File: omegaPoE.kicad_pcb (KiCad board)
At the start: 4 copper layers, 34 x 48 mm, 75 parts, among them J1 RJ45-TRANS_POE, J2 CONN_EXPANSION, J3 Conn_02x01, J4 Conn_02x01, Q1 FDM3622, SW1 SW_Push, T1 PA1276, U1 LM5070, U2 PS2501-1, U3 ONION-OMEGA2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

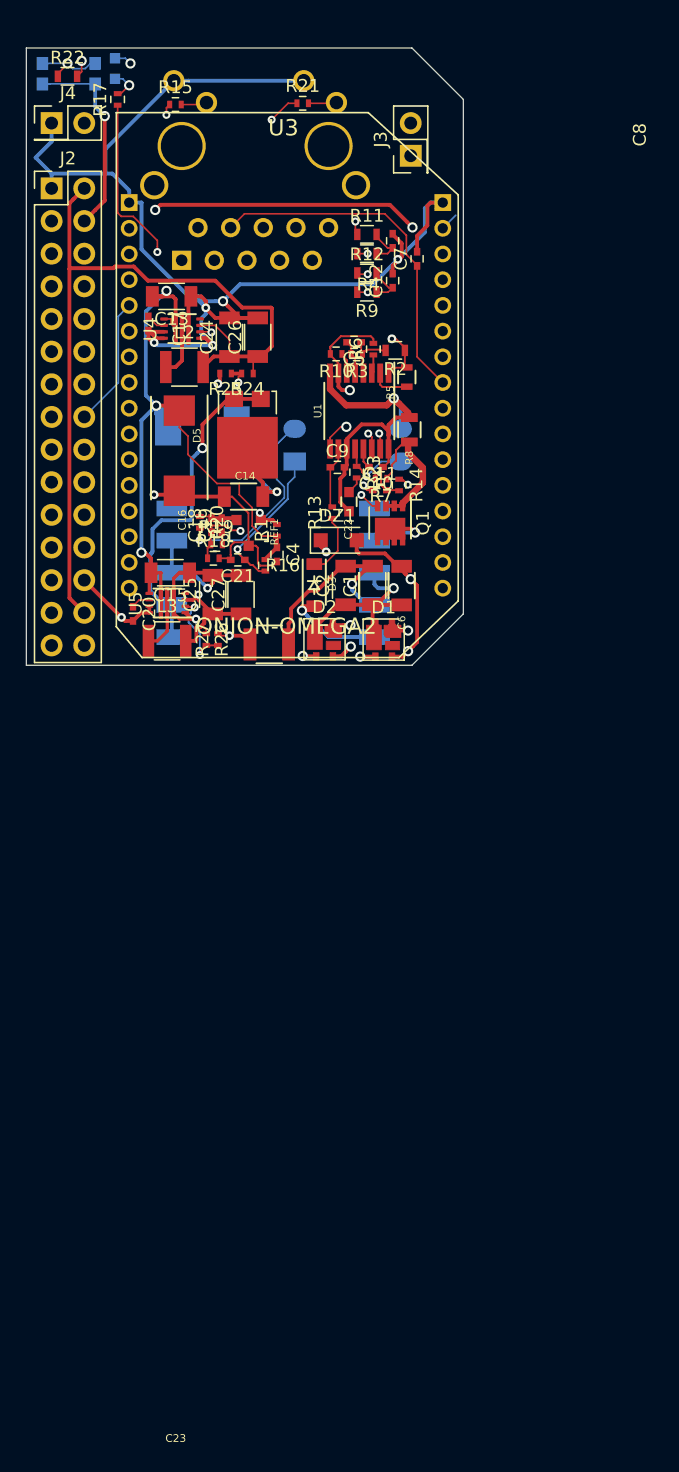
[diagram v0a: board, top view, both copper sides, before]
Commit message: More cleanup, some power planes in and text fixed
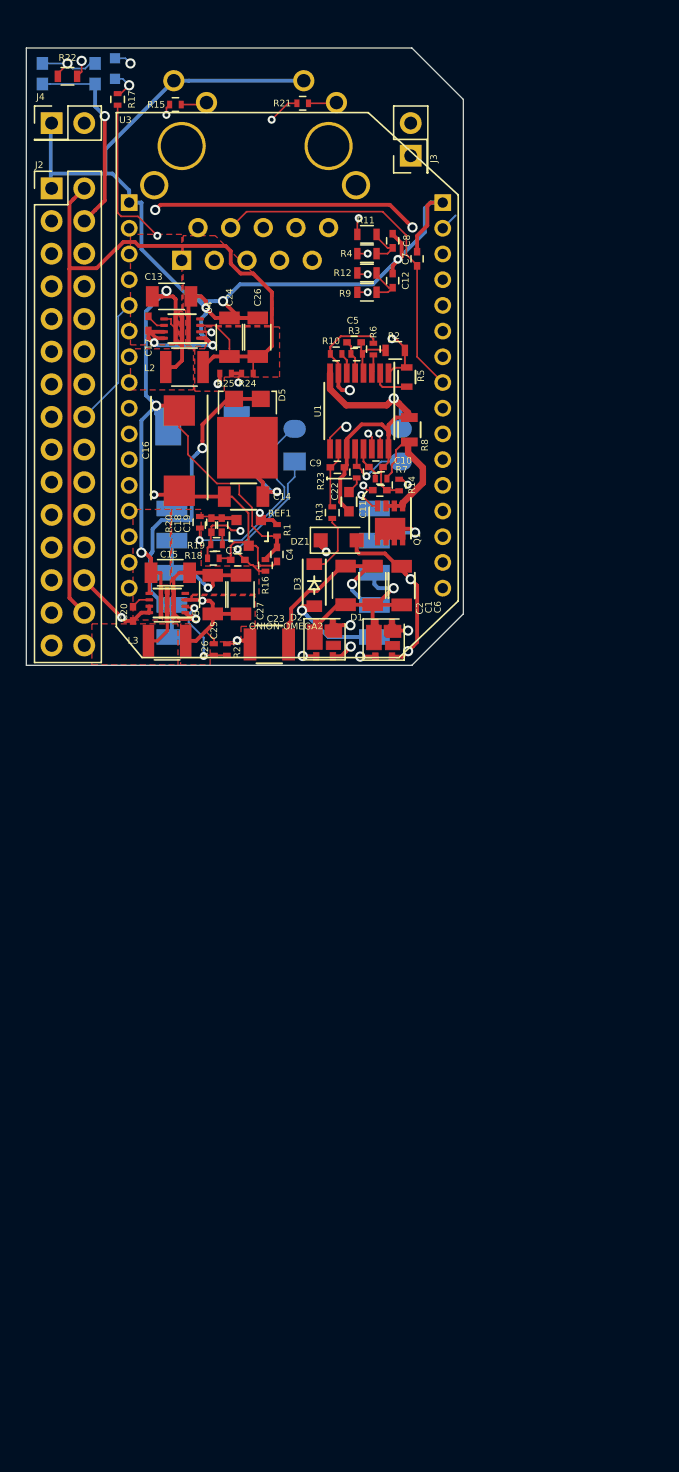
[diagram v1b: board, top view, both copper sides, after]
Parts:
- moved R27 1.04 mm to (98.6, 98.3)
- moved R26 0.98 mm to (97.6, 98.3)
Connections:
- J2 pad 5: Net-(J2-Pad5) -> (no net)
- U4 pad 7: (no net) -> Net-(U4-Pad7)
- U5 pad 7: (no net) -> Net-(U5-Pad7)
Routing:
- net /D+: track 31.5 -> 35.5 mm
- net +5V: track 65.6 -> 68.5 mm
- net /ETH_TD-: track 31.7 -> 33.6 mm
- net /ETH_TD+: track 35.8 -> 37.7 mm
- net /IO12: track 38.7 -> 40.4 mm
- net /D-: track 34.0 -> 35.3 mm
- net /ETH_RD+: track 33.2 -> 32.1 mm
- net /IO13: track 48.7 -> 49.7 mm
- net GND: track 196.2 -> 195.7 mm
- added copper zone on F.Cu, net +12V
- added copper zone on F.Cu, net +3V3
- added copper zone on F.Cu, net +5V
- added copper zone on F.Cu, net GND
- added copper zone on In1.Cu, net GND
- added copper zone on F.Cu, net Net-(L2-Pad1)
- added copper zone on F.Cu, net Net-(L3-Pad1)
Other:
- rule pad_to_mask_clearance: 0 -> 0.05
- rule via_min_size: 0.625 -> 0.56

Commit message: Mostly finished with design. Fixed lots of 3D models and some part rotations.
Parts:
- C16: footprint Capacitors_Tantalum_SMD:TantalC_SizeD_EIA-7343_Reflow -> Capacitors_Tantalum_SMD:CP_Tantalum_Case-D_EIA-7343-31_Reflow
- D1, D2: value D_Bridge_+-AA -> D_Bridge_A+A-
- D3: footprint Diodes_SMD:SOD-123 -> Diodes_SMD:D_SOD-123
- J3: moved to B.Cu
- L1: footprint inductors:Murata-3000A-series -> lib_fp:Murata-3000A-series
- REF1: footprint Housings_SOT-23_SOT-143_TSOT-6:SOT-23 -> TO_SOT_Packages_SMD:SOT-23
- T1: footprint ethernet_transformers:Pulse_PA1269 -> lib_fp:Pulse_PA1269
- U2: footprint DIP_Gull:DIP-Gull-4 -> Housings_DIP:SMDIP-4_W7.62mm
- moved U2 0.28 mm to (108.0, 82.1), turned to 0 degrees
- moved C18 0.14 mm to (97.3, 88.7)
- moved C19 0.14 mm to (98.1, 88.7)
- moved R19 0.14 mm to (97.7, 90.2)
- moved R20 0.14 mm to (96.4, 88.5)
- turned REF1 to 270 degrees
- turned D1 to 270 degrees
- turned D2 to 270 degrees
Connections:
- D1 pad 1: /Input_GND -> /Bridge1_2
- D1 pad 2: /Input-48V -> /Input_GND
- D1 pad 4: /Bridge1_2 -> /Input-48V
- D2 pad 1: /Input_GND -> /Bridge2_2
- D2 pad 2: /Input-48V -> /Input_GND
- D2 pad 4: /Bridge2_2 -> /Input-48V
- J2 pad 5: (no net) -> Net-(J2-Pad5)
- U4 pad 7: Net-(U4-Pad7) -> (no net)
- U5 pad 7: Net-(U5-Pad7) -> (no net)
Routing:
- net Net-(R20-Pad2): track 15.2 -> 16.9 mm
- net Net-(C21-Pad1): track 11.7 -> 12.9 mm
- net /fetdrive: track 10.1 -> 10.5 mm, vias 2 -> 0

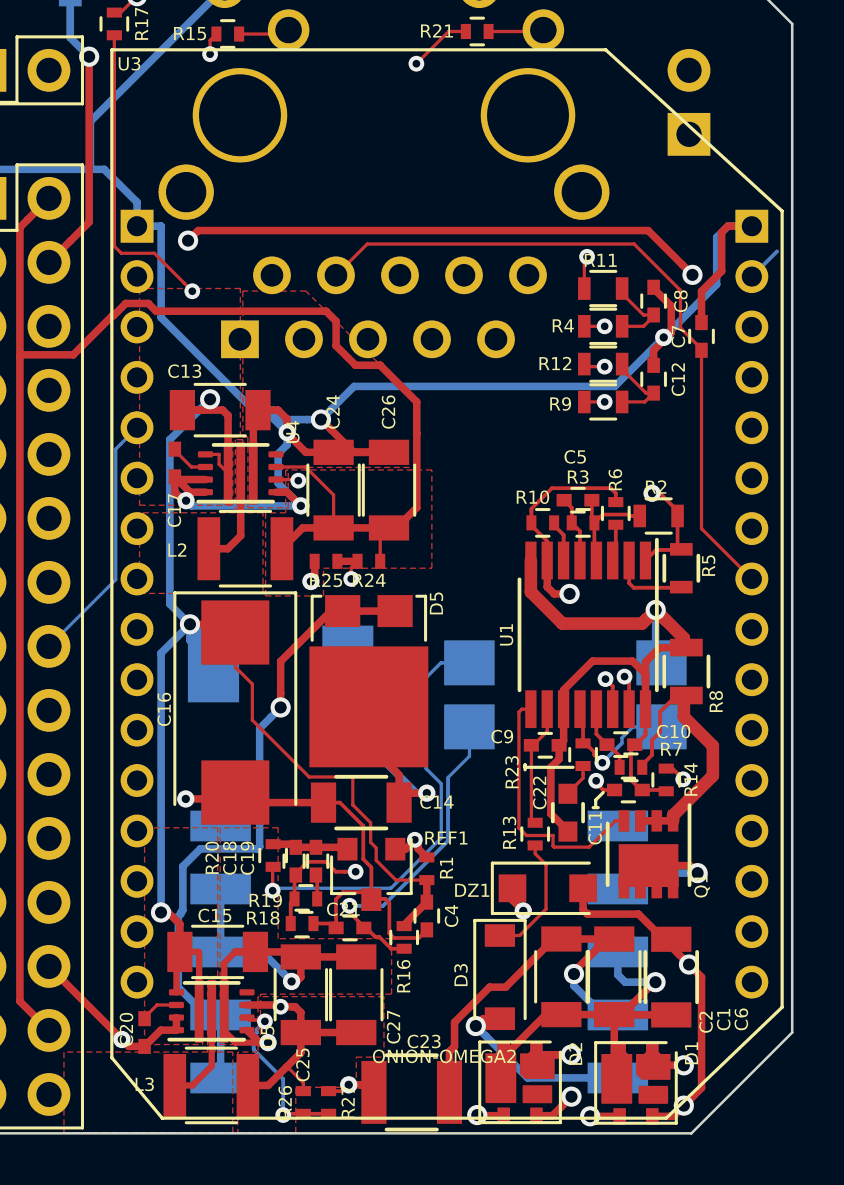
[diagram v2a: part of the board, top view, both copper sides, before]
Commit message: Swapped to some cheaper parts, fixed cap selection on 12V line.
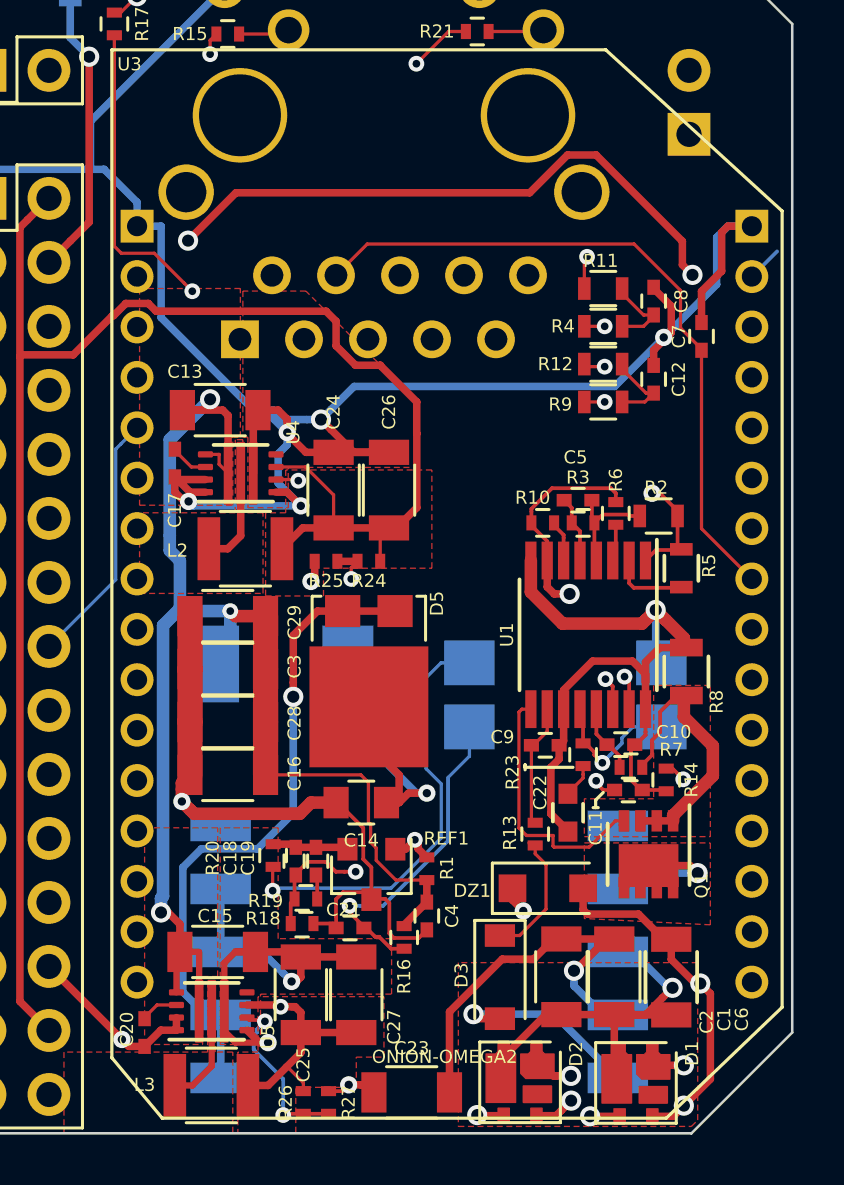
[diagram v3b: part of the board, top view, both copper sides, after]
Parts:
- added C28: 10uF, Capacitors_SMD:C_1206, F.Cu at (94.6, 83.2)
- added C29: 10uF, Capacitors_SMD:C_1206, F.Cu at (94.6, 79.0)
- added C3: 10uF, Capacitors_SMD:C_1206, F.Cu at (94.6, 81.1)
- C14: value 47uF -> 4.7uF; footprint Capacitors_SMD:C_1206 -> Capacitors_SMD:C_0805
- C16: value 390uF -> 10uF; footprint Capacitors_Tantalum_SMD:CP_Tantalum_Case-D_EIA-7343-31_Reflow -> Capacitors_SMD:C_1206
- C23: footprint Capacitors_SMD:C_1210 -> Capacitors_SMD:C_1206
- C4: value 1uF -> 100nF
- moved C16 2.49 mm to (94.6, 85.3), turned to 0 degrees
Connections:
- C16 pad 1: +12V -> GND
- C16 pad 2: GND -> +12V
- J2 pad 5: Net-(J2-Pad5) -> (no net)
- U4 pad 7: (no net) -> Net-(U4-Pad7)
- U5 pad 7: (no net) -> Net-(U5-Pad7)
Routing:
- net GND: track 195.7 -> 202.7 mm
- net /IO18: track 34.4 -> 39.8 mm
- net /IO19: track 32.5 -> 37.1 mm
- net /Input-48V: track 51.6 -> 56.1 mm
- net /IO4: track 30.8 -> 34.5 mm
- net +12V: track 74.7 -> 77.7 mm
- net +3V3: track 103.5 -> 106.5 mm
- net /IO5: track 30.0 -> 32.6 mm
- net /Input_GND: track 65.9 -> 67.5 mm
- net /Bridge2_2: track 31.0 -> 32.1 mm
- net GNDA: track 88.0 -> 87.1 mm
- net /output_pre_choke: track 12.2 -> 12.7 mm
- added copper zone on F.Cu, net /Input_GND
- added copper zone on F.Cu, net /coil_to_fet
- added copper zone on F.Cu, net /pre_curr_sense
- added copper zone on In1.Cu, net GNDA
- added copper zone on In2.Cu, net GNDA

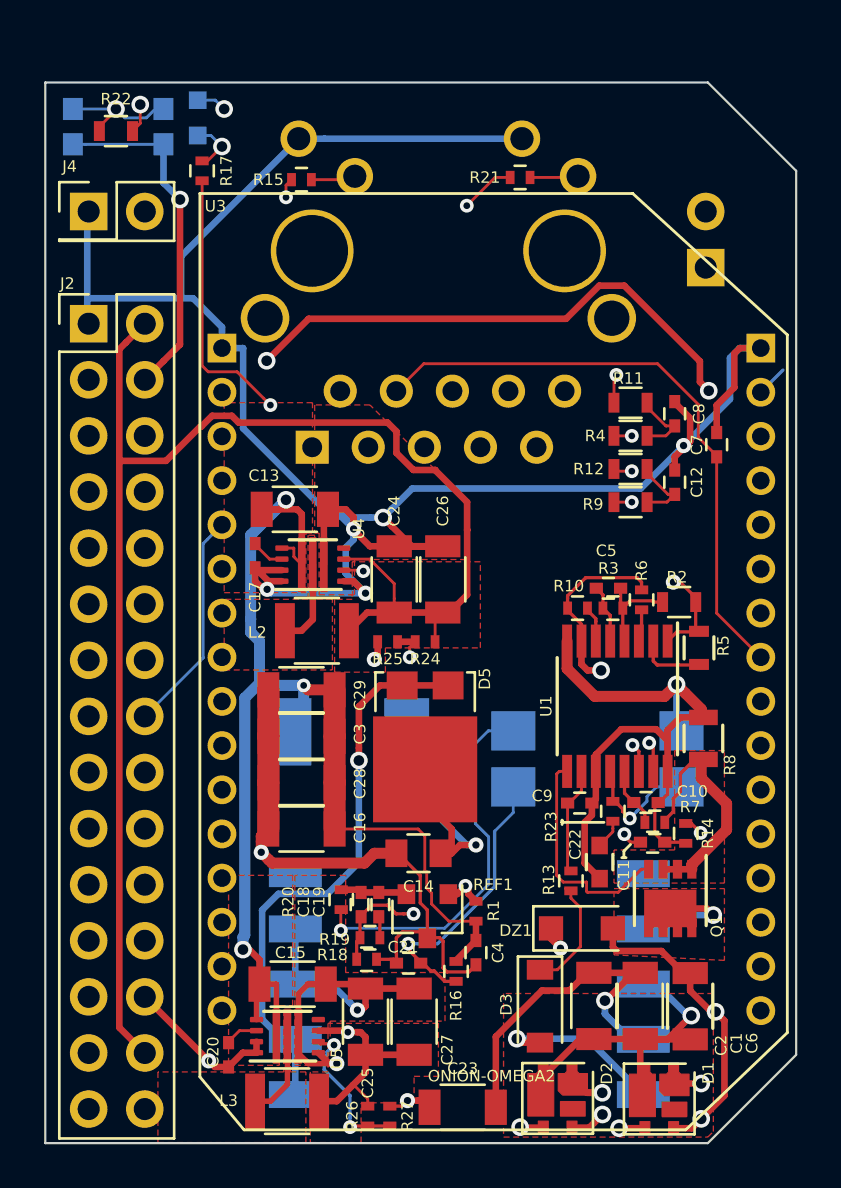
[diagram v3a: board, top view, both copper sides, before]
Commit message: Added mounting holes, shrank up board, make 12V output switched
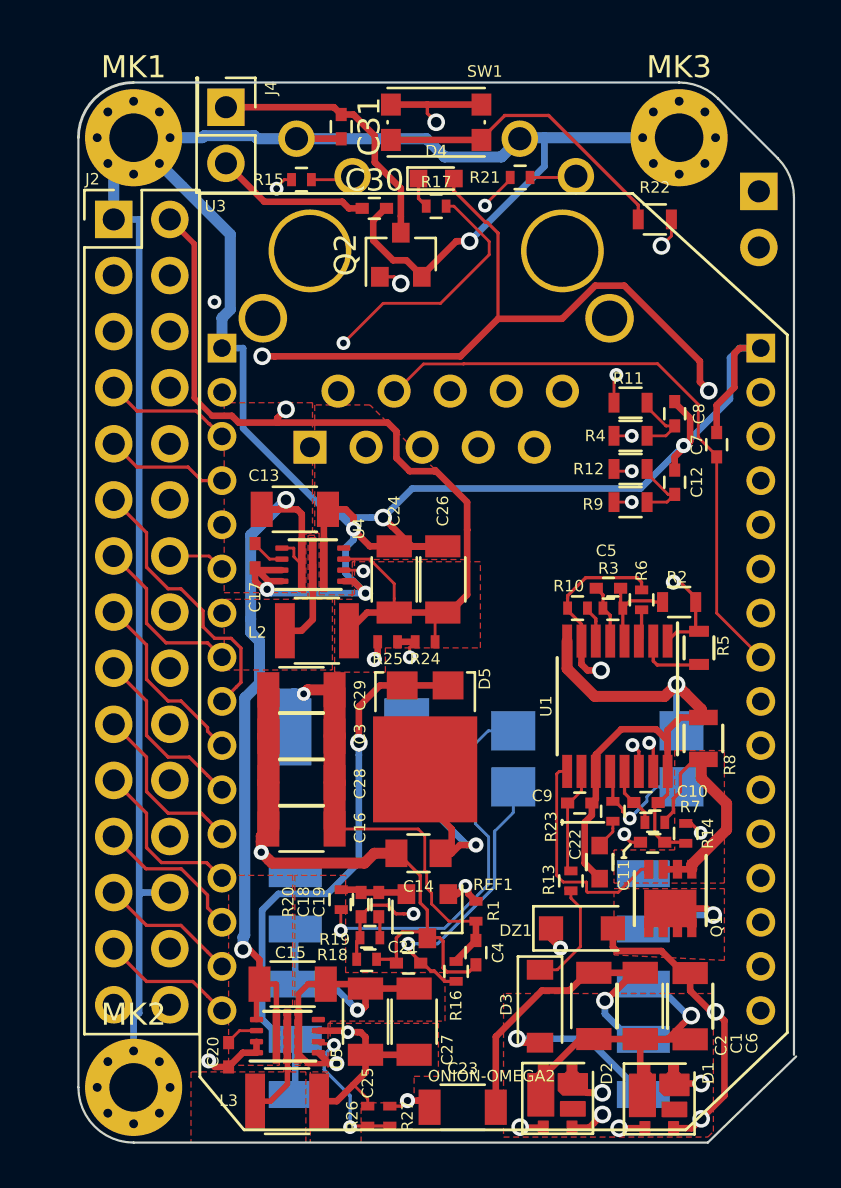
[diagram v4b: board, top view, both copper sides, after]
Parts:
- added C30: 1uF, Capacitors_SMD:C_0402, F.Cu at (97.9, 57.2)
- added C31: 1uF, Capacitors_SMD:C_0402, F.Cu at (96.4, 53.5)
- added MK1: Hole, Mounting_Holes:MountingHole_2.2mm_M2_Pad_Via, F.Cu at (87.0, 54.0)
- added MK2: Hole, Mounting_Holes:MountingHole_2.2mm_M2_Pad_Via, F.Cu at (87.0, 97.0)
- added MK3: Hole, Mounting_Holes:MountingHole_2.2mm_M2_Pad_Via, F.Cu at (111.7, 54.0)
- added Q2: Q_NMOS_GSD, TO_SOT_Packages_SMD:SOT-23, F.Cu at (99.1, 59.3)
- D4, SW1: moved to F.Cu
- moved R22 24.7 mm to (110.6, 57.7)
- moved SW1 14.4 mm to (100.7, 53.3)
- moved D4 11.1 mm to (100.7, 55.9), turned to 0 degrees
- moved R17 10.7 mm to (100.7, 57.1), turned to 180 degrees
- moved J4 7.81 mm to (91.2, 52.6), turned to 270 degrees
- moved J2 4.86 mm to (86.1, 57.7)
- moved J3 4.21 mm to (115.3, 56.4), turned to 270 degrees
- moved J1 0.10 mm to (100.7, 59.1)
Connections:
- J4 pad 1: GND -> Net-(C31-Pad1)
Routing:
- net GND: track 202.7 -> 261.3 mm, vias 11 -> 12
- net /IO18: track 39.8 -> 75.9 mm, vias 0 -> 1
- net /RESET_BUTTON: track 50.4 -> 22.2 mm
- net +3V3: track 106.5 -> 92.9 mm, vias 4 -> 3
- net Net-(C31-Pad1): track 0.00 -> 12.1 mm
- net /IO16: track 43.3 -> 34.2 mm
- net Net-(R22-Pad1): track 5.74 -> 14.0 mm, vias 1 -> 0
- net /VDD25: track 22.9 -> 30.8 mm, vias 1 -> 2
- net /IO13: track 49.7 -> 43.3 mm
- net +12V: track 77.7 -> 83.7 mm
- net /IO19: track 37.1 -> 31.8 mm
- net /Input_GND: track 67.5 -> 72.7 mm
- net /IO15: track 35.7 -> 30.8 mm
- net /IO45: track 12.6 -> 7.71 mm
- net /IO46: track 8.99 -> 12.6 mm
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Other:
- board size 34 x 48 mm -> 32.5 x 48 mm
